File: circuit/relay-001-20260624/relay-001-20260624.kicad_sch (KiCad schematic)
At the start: 14 parts, among them J1 Conn_01x03_Pin, J10 Conn_01x02_Pin, J11 Conn_01x02_Pin, J12 Conn_01x02_Pin, J13 Conn_01x02_Pin, J14 Conn_01x02_Pin, J2 Conn_02x05_Odd_Even, J3 Conn_02x08_Odd_Even, J4 Conn_02x09_Odd_Even, J5 Conn_01x02_Pin, J6 Conn_01x02_Pin, J7 Conn_01x02_Pin, J8 Conn_01x02_Pin, J9 Conn_01x02_Pin

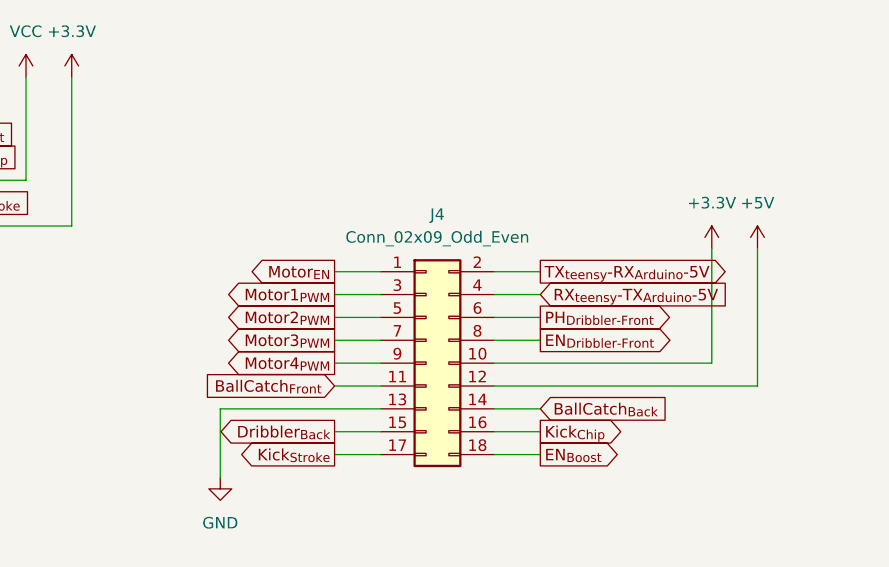
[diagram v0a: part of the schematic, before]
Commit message: Update 供給基板の回路図を更新
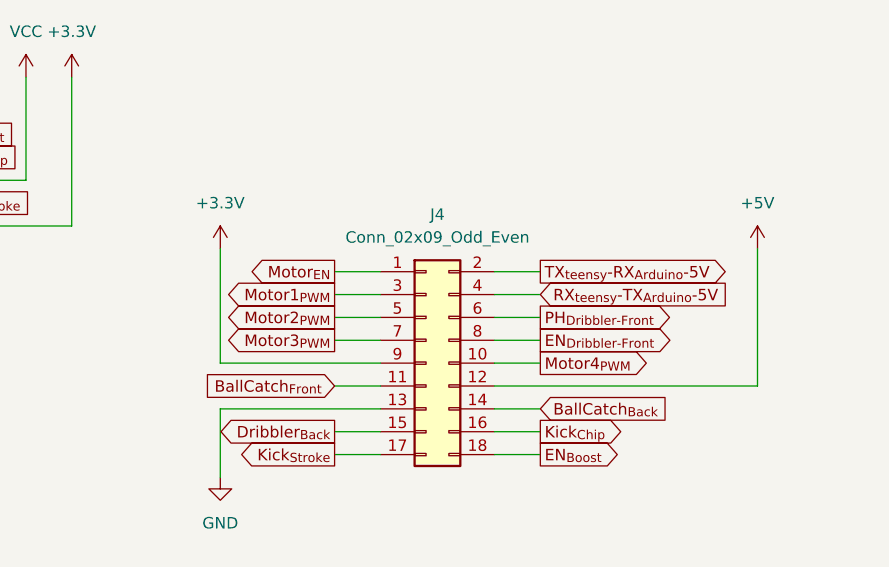
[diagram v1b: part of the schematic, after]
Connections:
- net +3.3V: now also J4.9 (Pin_9); no longer J4.10 (Pin_10)
- net Motor4_{PWM}: now also J4.10 (Pin_10); no longer J4.9 (Pin_9)
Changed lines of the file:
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@@
 	(wire
 		(pts
+			(xy 220.98 95.25) (xy 203.2 95.25)
+		)
+		(stroke
+			(width 0)
+			(type default)
+		)
+	)
+	(wire
+		(pts
 			(xy 148.59 72.39) (xy 153.67 72.39)
 		)
@@
 	(wire
 		(pts
-			(xy 215.9 95.25) (xy 220.98 95.25)
+			(xy 238.76 95.25) (xy 233.68 95.25)
 		)
 		(stroke
@@
 	(wire
 		(pts
-			(xy 257.81 82.55) (xy 257.81 95.25)
-		)
-		(stroke
-			(width 0)
-			(type default)
-		)
-	)
-	(wire
-		(pts
 			(xy 238.76 85.09) (xy 233.68 85.09)
 		)
@@
 	(wire
 		(pts
+			(xy 203.2 82.55) (xy 203.2 95.25)
+		)
+		(stroke
+			(width 0)
+			(type default)
+		)
+	)
+	(wire
+		(pts
 			(xy 172.72 144.78) (xy 177.8 144.78)
 		)
@@
 	(wire
 		(pts
-			(xy 233.68 95.25) (xy 257.81 95.25)
-		)
-		(stroke
-			(width 0)
-			(type default)
-		)
-	)
-	(wire
-		(pts
 			(xy 238.76 102.87) (xy 233.68 102.87)
 		)
@@
 	(global_label "Motor4_{PWM}"
 		(shape output)
-		(at 215.9 95.25 180)
+		(at 238.76 95.25 0)
 		(fields_autoplaced yes)
 		(effects
@@
 				(size 1.27 1.27)
 			)
-			(justify right)
+			(justify left)
 		)
 		(property "Intersheetrefs" "${INTERSHEET_REFS}"
-			(at 204.8305 95.25 0)
+			(at 249.8295 95.25 0)
 			(hide yes)
 			(show_name no)
@@
 					(size 1.27 1.27)
 				)
-				(justify right)
+				(justify left)
 			)
 		)
@@
 		)
 		(instances
-			(project "powerline-001-2026-624"
+			(project "relay-001-20260624"
 				(path "/3563ad31-a35a-4c8c-920a-9f3c7338d38d"
 					(reference "#PWR06")
@@
 		)
 		(instances
-			(project "powerline-001-2026-624"
+			(project "relay-001-20260624"
 				(path "/3563ad31-a35a-4c8c-920a-9f3c7338d38d"
 					(reference "J2")
@@
 		)
 		(instances
-			(project "powerline-001-2026-624"
+			(project "relay-001-20260624"
 				(path "/3563ad31-a35a-4c8c-920a-9f3c7338d38d"
 					(reference "J9")
@@
 		)
 		(instances
-			(project "powerline-001-2026-624"
+			(project "relay-001-20260624"
 				(path "/3563ad31-a35a-4c8c-920a-9f3c7338d38d"
 					(reference "J14")
@@
 		)
 		(instances
-			(project "powerline-001-2026-624"
+			(project "relay-001-20260624"
 				(path "/3563ad31-a35a-4c8c-920a-9f3c7338d38d"
 					(reference "#PWR015")
@@
 		)
 		(instances
-			(project "powerline-001-2026-624"
+			(project "relay-001-20260624"
 				(path "/3563ad31-a35a-4c8c-920a-9f3c7338d38d"
 					(reference "J12")
@@
 		)
 		(instances
-			(project "powerline-001-2026-624"
+			(project "relay-001-20260624"
 				(path "/3563ad31-a35a-4c8c-920a-9f3c7338d38d"
 					(reference "#PWR011")
@@
 		)
 		(instances
-			(project "powerline-001-2026-624"
+			(project "relay-001-20260624"
 				(path "/3563ad31-a35a-4c8c-920a-9f3c7338d38d"
 					(reference "#PWR018")
@@
 		)
 		(instances
-			(project "powerline-001-2026-624"
+			(project "relay-001-20260624"
 				(path "/3563ad31-a35a-4c8c-920a-9f3c7338d38d"
 					(reference "#PWR017")
@@
 		)
 		(instances
-			(project "powerline-001-2026-624"
+			(project "relay-001-20260624"
 				(path "/3563ad31-a35a-4c8c-920a-9f3c7338d38d"
 					(reference "#PWR01")
@@
 		)
 		(instances
-			(project "powerline-001-2026-624"
+			(project "relay-001-20260624"
 				(path "/3563ad31-a35a-4c8c-920a-9f3c7338d38d"
 					(reference "J11")
@@
 		)
 		(instances
-			(project "powerline-001-2026-624"
+			(project "relay-001-20260624"
 				(path "/3563ad31-a35a-4c8c-920a-9f3c7338d38d"
 					(reference "J13")
@@
 		)
 		(instances
-			(project "powerline-001-2026-624"
+			(project "relay-001-20260624"
 				(path "/3563ad31-a35a-4c8c-920a-9f3c7338d38d"
 					(reference "J3")
@@
 		)
 		(instances
-			(project "powerline-001-2026-624"
+			(project "relay-001-20260624"
 				(path "/3563ad31-a35a-4c8c-920a-9f3c7338d38d"
 					(reference "J4")
@@
 		)
 		(instances
-			(project "powerline-001-2026-624"
+			(project "relay-001-20260624"
 				(path "/3563ad31-a35a-4c8c-920a-9f3c7338d38d"
 					(reference "#PWR02")
@@
 		)
 		(instances
-			(project "powerline-001-2026-624"
+			(project "relay-001-20260624"
 				(path "/3563ad31-a35a-4c8c-920a-9f3c7338d38d"
 					(reference "#PWR03")
@@
 		)
 		(instances
-			(project "powerline-001-2026-624"
+			(project "relay-001-20260624"
 				(path "/3563ad31-a35a-4c8c-920a-9f3c7338d38d"
 					(reference "#PWR08")
@@
 		)
 		(instances
-			(project "powerline-001-2026-624"
+			(project "relay-001-20260624"
 				(path "/3563ad31-a35a-4c8c-920a-9f3c7338d38d"
 					(reference "J10")
@@
 		)
 		(instances
-			(project "powerline-001-2026-624"
+			(project "relay-001-20260624"
 				(path "/3563ad31-a35a-4c8c-920a-9f3c7338d38d"
 					(reference "#PWR013")
@@
 		)
 		(instances
-			(project "powerline-001-2026-624"
+			(project "relay-001-20260624"
 				(path "/3563ad31-a35a-4c8c-920a-9f3c7338d38d"
 					(reference "J1")
@@
 		)
 		(instances
-			(project "powerline-001-2026-624"
+			(project "relay-001-20260624"
 				(path "/3563ad31-a35a-4c8c-920a-9f3c7338d38d"
 					(reference "#PWR012")
@@
 		)
 		(instances
-			(project "powerline-001-2026-624"
+			(project "relay-001-20260624"
 				(path "/3563ad31-a35a-4c8c-920a-9f3c7338d38d"
 					(reference "J8")
@@
 		)
 		(instances
-			(project "powerline-001-2026-624"
+			(project "relay-001-20260624"
 				(path "/3563ad31-a35a-4c8c-920a-9f3c7338d38d"
 					(reference "#PWR010")
@@
 		)
 		(instances
-			(project "powerline-001-2026-624"
+			(project "relay-001-20260624"
 				(path "/3563ad31-a35a-4c8c-920a-9f3c7338d38d"
 					(reference "#PWR07")
@@
 		)
 		(instances
-			(project "powerline-001-2026-624"
+			(project "relay-001-20260624"
 				(path "/3563ad31-a35a-4c8c-920a-9f3c7338d38d"
 					(reference "#PWR014")
@@
 		)
 		(instances
-			(project "powerline-001-2026-624"
+			(project "relay-001-20260624"
 				(path "/3563ad31-a35a-4c8c-920a-9f3c7338d38d"
 					(reference "#PWR09")
@@
 		)
 		(instances
-			(project "powerline-001-2026-624"
+			(project "relay-001-20260624"
 				(path "/3563ad31-a35a-4c8c-920a-9f3c7338d38d"
 					(reference "J5")
@@
 		)
 		(instances
-			(project "powerline-001-2026-624"
+			(project "relay-001-20260624"
 				(path "/3563ad31-a35a-4c8c-920a-9f3c7338d38d"
 					(reference "#PWR016")
@@
 		)
 		(instances
-			(project "powerline-001-2026-624"
+			(project "relay-001-20260624"
 				(path "/3563ad31-a35a-4c8c-920a-9f3c7338d38d"
 					(reference "J7")
@@
 	(symbol
 		(lib_id "power:+3.3V")
-		(at 257.81 82.55 0)
+		(at 203.2 82.55 0)
 		(unit 1)
 		(body_style 1)
@@
 		(fields_autoplaced yes)
 		(property "Reference" "#PWR04"
-			(at 257.81 86.36 0)
+			(at 203.2 86.36 0)
 			(hide yes)
 			(show_name no)
@@
 		)
 		(property "Value" "+3.3V"
-			(at 257.81 77.47 0)
+			(at 203.2 77.47 0)
 			(show_name no)
 			(do_not_autoplace no)
@@
 		)
 		(property "Footprint" ""
-			(at 257.81 82.55 0)
+			(at 203.2 82.55 0)
 			(hide yes)
 			(show_name no)
@@
 		)
 		(property "Datasheet" ""
-			(at 257.81 82.55 0)
+			(at 203.2 82.55 0)
 			(hide yes)
 			(show_name no)
@@
 		)
 		(property "Description" "Power symbol creates a global label with name \"+3.3V\""
-			(at 257.81 82.55 0)
+			(at 203.2 82.55 0)
 			(hide yes)
 			(show_name no)
@@
 		)
 		(instances
-			(project "powerline-001-2026-624"
+			(project "relay-001-20260624"
 				(path "/3563ad31-a35a-4c8c-920a-9f3c7338d38d"
 					(reference "#PWR04")
@@
 		)
 		(instances
-			(project "powerline-001-2026-624"
+			(project "relay-001-20260624"
 				(path "/3563ad31-a35a-4c8c-920a-9f3c7338d38d"
 					(reference "J6")
@@
 		)
 		(instances
-			(project "powerline-001-2026-624"
+			(project "relay-001-20260624"
 				(path "/3563ad31-a35a-4c8c-920a-9f3c7338d38d"
 					(reference "#PWR05")

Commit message: Update 供給基板のボード図を進めた
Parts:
- added J15: Conn_01x02_Pin, Connector_JST:JST_XH_B2B-XH-A_1x02_P2.50mm_Vertical, symbol Connector:Conn_01x02_Pin
- J1: footprint (none) -> Connector_PinHeader_2.54mm:PinHeader_1x03_P2.54mm_Vertical
- J10: footprint (none) -> Connector_AMASS:AMASS_XT30PW-M_1x02_P2.50mm_Horizontal
- J11, J12, J13, J14, J9: footprint (none) -> Connector_JST:JST_XH_B2B-XH-A_1x02_P2.50mm_Vertical
- J2: footprint (none) -> Connector_PinSocket_2.54mm:PinSocket_2x05_P2.54mm_Vertical
- J3: footprint (none) -> Connector_PinSocket_2.54mm:PinSocket_2x08_P2.54mm_Horizontal
- J4: footprint (none) -> Connector_PinSocket_2.54mm:PinSocket_2x09_P2.54mm_Vertical
- J5, J6, J7, J8: footprint (none) -> Connector_AMASS:AMASS_XT30U-M_1x02_P5.0mm_Vertical
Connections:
- net GND: now also J15.2 (Pin_2)
- net VCC: now also J15.1 (Pin_1)
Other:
- moved on the sheet: J1, J11, J12, J13, J14

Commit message: Update 供給基板のボード図を進めた
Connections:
- net +3.3V: now also J2.9 (Pin_9), J3.13 (Pin_13), J7.1 (Pin_1); no longer J2.10 (Pin_10), J3.2 (Pin_2), J7.2 (Pin_2)
- net +5V: now also J7.2 (Pin_2); no longer J7.1 (Pin_1)
- net +5V_{Line}: now also J5.2 (Pin_2), J8.2 (Pin_2); no longer J5.1 (Pin_1), J8.1 (Pin_1)
- net BallCatch_{Back}: now also J3.1 (Pin_1); no longer J3.16 (Pin_16)
- net BallCatch_{Front}: now also J2.8 (Pin_8); no longer J2.7 (Pin_7)
- net EN_{Boost}: now also J2.1 (Pin_1); no longer J2.2 (Pin_2)
- net EN_{Dribbler-Front}: now also J2.4 (Pin_4); no longer J2.3 (Pin_3)
- net GND: now also J10.1 (Pin_1), J2.10 (Pin_10), J2.2 (Pin_2), J3.15 (Pin_15), J5.1 (Pin_1), J6.1 (Pin_1), J8.1 (Pin_1); no longer J10.2 (Pin_2), J2.1 (Pin_1), J2.9 (Pin_9), J3.4 (Pin_4), J5.2 (Pin_2), J6.2 (Pin_2), J8.2 (Pin_2)
- net Kick_{Chip}: now also J2.3 (Pin_3); no longer J2.4 (Pin_4)
- net Kick_{Stroke}: now also J2.7 (Pin_7); no longer J2.8 (Pin_8)
- net Motor1_{PWM}: now also J3.9 (Pin_9); no longer J3.8 (Pin_8)
- net Motor2_{PWM}: now also J3.7 (Pin_7); no longer J3.10 (Pin_10)
- net Motor3_{PWM}: now also J3.5 (Pin_5); no longer J3.12 (Pin_12)
- net Motor4_{PWM}: now also J3.3 (Pin_3); no longer J3.14 (Pin_14)
- net Motor_{EN}: now also J3.11 (Pin_11); no longer J3.6 (Pin_6)
- net Motor_{OUT1-1}: now also J3.16 (Pin_16); no longer J3.1 (Pin_1)
- net Motor_{OUT1-2}: now also J3.14 (Pin_14); no longer J3.3 (Pin_3)
- net Motor_{OUT2-1}: now also J3.12 (Pin_12); no longer J3.5 (Pin_5)
- net Motor_{OUT2-2}: now also J3.10 (Pin_10); no longer J3.7 (Pin_7)
- net Motor_{OUT3-1}: now also J3.8 (Pin_8); no longer J3.9 (Pin_9)
- net Motor_{OUT3-2}: now also J3.6 (Pin_6); no longer J3.11 (Pin_11)
- net Motor_{OUT4-1}: now also J3.4 (Pin_4); no longer J3.13 (Pin_13)
- net Motor_{OUT4-2}: now also J3.2 (Pin_2); no longer J3.15 (Pin_15)
- net PH_{Dribbler-Front}: now also J2.6 (Pin_6); no longer J2.5 (Pin_5)
- net VCC: now also J10.2 (Pin_2), J2.5 (Pin_5), J6.2 (Pin_2); no longer J10.1 (Pin_1), J2.6 (Pin_6), J6.1 (Pin_1)
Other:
- moved on the sheet: J10, J2, J3, J5, J6, J7, J8

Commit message: Update 供給基板のボード図を更新
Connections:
- net +3.3V: now also J3.15 (Pin_15); no longer J3.13 (Pin_13)
- net GND: now also J3.13 (Pin_13); no longer J3.15 (Pin_15)
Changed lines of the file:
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@@
 	(wire
 		(pts
-			(xy 147.32 144.78) (xy 147.32 148.59)
+			(xy 148.59 149.86) (xy 148.59 151.13)
 		)
 		(stroke
@@
 	(wire
 		(pts
-			(xy 147.32 148.59) (xy 167.64 148.59)
+			(xy 148.59 151.13) (xy 167.64 151.13)
 		)
 		(stroke
@@
 	(wire
 		(pts
-			(xy 147.32 151.13) (xy 167.64 151.13)
+			(xy 152.4 148.59) (xy 167.64 148.59)
 		)
 		(stroke
@@
 	(wire
 		(pts
-			(xy 147.32 151.13) (xy 147.32 154.94)
+			(xy 152.4 148.59) (xy 152.4 152.4)
 		)
 		(stroke
@@
 	(symbol
 		(lib_id "power:GND")
-		(at 147.32 154.94 0)
+		(at 152.4 152.4 0)
 		(unit 1)
 		(body_style 1)
@@
 		(fields_autoplaced yes)
 		(property "Reference" "#PWR08"
-			(at 147.32 161.29 0)
+			(at 152.4 158.75 0)
 			(hide yes)
 			(show_name no)
@@
 		)
 		(property "Value" "GND"
-			(at 147.32 160.02 0)
+			(at 152.4 157.48 0)
 			(show_name no)
 			(do_not_autoplace no)
@@
 		)
 		(property "Footprint" ""
-			(at 147.32 154.94 0)
+			(at 152.4 152.4 0)
 			(hide yes)
 			(show_name no)
@@
 		)
 		(property "Datasheet" ""
-			(at 147.32 154.94 0)
+			(at 152.4 152.4 0)
 			(hide yes)
 			(show_name no)
@@
 		)
 		(property "Description" "Power symbol creates a global label with name \"GND\" , ground"
-			(at 147.32 154.94 0)
+			(at 152.4 152.4 0)
 			(hide yes)
 			(show_name no)
@@
 	(symbol
 		(lib_id "power:+3.3V")
-		(at 147.32 144.78 0)
+		(at 148.59 149.86 0)
 		(unit 1)
 		(body_style 1)
@@
 		(fields_autoplaced yes)
 		(property "Reference" "#PWR07"
-			(at 147.32 148.59 0)
+			(at 148.59 153.67 0)
 			(hide yes)
 			(show_name no)
@@
 		)
 		(property "Value" "+3.3V"
-			(at 147.32 139.7 0)
+			(at 148.59 144.78 0)
 			(show_name no)
 			(do_not_autoplace no)
@@
 		)
 		(property "Footprint" ""
-			(at 147.32 144.78 0)
+			(at 148.59 149.86 0)
 			(hide yes)
 			(show_name no)
@@
 		)
 		(property "Datasheet" ""
-			(at 147.32 144.78 0)
+			(at 148.59 149.86 0)
 			(hide yes)
 			(show_name no)
@@
 		)
 		(property "Description" "Power symbol creates a global label with name \"+3.3V\""
-			(at 147.32 144.78 0)
+			(at 148.59 149.86 0)
 			(hide yes)
 			(show_name no)

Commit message: Update 供給基板を開いてちょっとシルクスクリーンを修正
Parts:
- J1: value Conn_01x03_Pin -> Dribbler_{Back}
- J11: value Conn_01x02_Pin -> Motor1
- J12: value Conn_01x02_Pin -> Motor2
- J13: value Conn_01x02_Pin -> Motor3
- J14: value Conn_01x02_Pin -> Motor4
- J2: value Conn_02x05_Odd_Even -> Kicker-Board
- J3: value Conn_02x08_Odd_Even -> MD-Board
- J4: value Conn_02x09_Odd_Even -> Main-Board
- J5, J8: value Conn_01x02_Pin -> Linesensor_{Power}
- J9: value Conn_01x02_Pin -> Linesensor_{UART}
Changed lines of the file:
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@@
 			)
 		)
-		(property "Value" "Conn_02x05_Odd_Even"
+		(property "Value" "Kicker-Board"
 			(at 172.72 52.07 0)
 			(show_name no)
@@
 			)
 		)
-		(property "Value" "Conn_01x02_Pin"
+		(property "Value" "Linesensor_{UART}"
 			(at 225.425 40.64 0)
 			(show_name no)
@@
 			)
 		)
-		(property "Value" "Conn_01x02_Pin"
+		(property "Value" "Motor4"
 			(at 37.465 113.03 0)
 			(show_name no)
@@
 			)
 		)
-		(property "Value" "Conn_01x02_Pin"
+		(property "Value" "Motor2"
 			(at 37.465 87.63 0)
 			(show_name no)
@@
 			)
 		)
-		(property "Value" "Conn_01x02_Pin"
+		(property "Value" "Motor1"
 			(at 37.465 74.93 0)
 			(show_name no)
@@
 			)
 		)
-		(property "Value" "Conn_01x02_Pin"
+		(property "Value" "Motor3"
 			(at 37.465 100.33 0)
 			(show_name no)
@@
 			)
 		)
-		(property "Value" "Conn_02x08_Odd_Even"
+		(property "Value" "MD-Board"
 			(at 173.99 129.54 0)
 			(show_name no)
@@
 			)
 		)
-		(property "Value" "Conn_02x09_Odd_Even"
+		(property "Value" "Main-Board"
 			(at 227.33 81.28 0)
 			(show_name no)
@@
 			)
 		)
-		(property "Value" "Conn_01x03_Pin"
+		(property "Value" "Dribbler_{Back}"
 			(at 31.115 26.67 0)
 			(show_name no)
@@
 		(fields_autoplaced yes)
 		(property "Reference" "J8"
-			(at 247.65 25.4 0)
+			(at 247.65 25.3999 0)
 			(show_name no)
 			(do_not_autoplace no)
@@
 			)
 		)
-		(property "Value" "Conn_01x02_Pin"
-			(at 247.65 27.94 0)
+		(property "Value" "Linesensor_{Power}"
+			(at 247.65 27.9399 0)
 			(show_name no)
 			(do_not_autoplace no)
@@
 		(fields_autoplaced yes)
 		(property "Reference" "J5"
-			(at 111.76 74.93 0)
+			(at 111.76 74.9299 0)
 			(show_name no)
 			(do_not_autoplace no)
@@
 			)
 		)
-		(property "Value" "Conn_01x02_Pin"
-			(at 111.76 77.47 0)
-			(show_name no)
-			(do_not_autoplace no)
+		(property "Value" "Linesensor_{Power}"
+			(at 111.76 77.4699 0)
+			(show_name no)
+			(do_not_autoplace no)
